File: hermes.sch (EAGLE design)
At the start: 49 parts, among them IC1 MIC5219-3.3BML

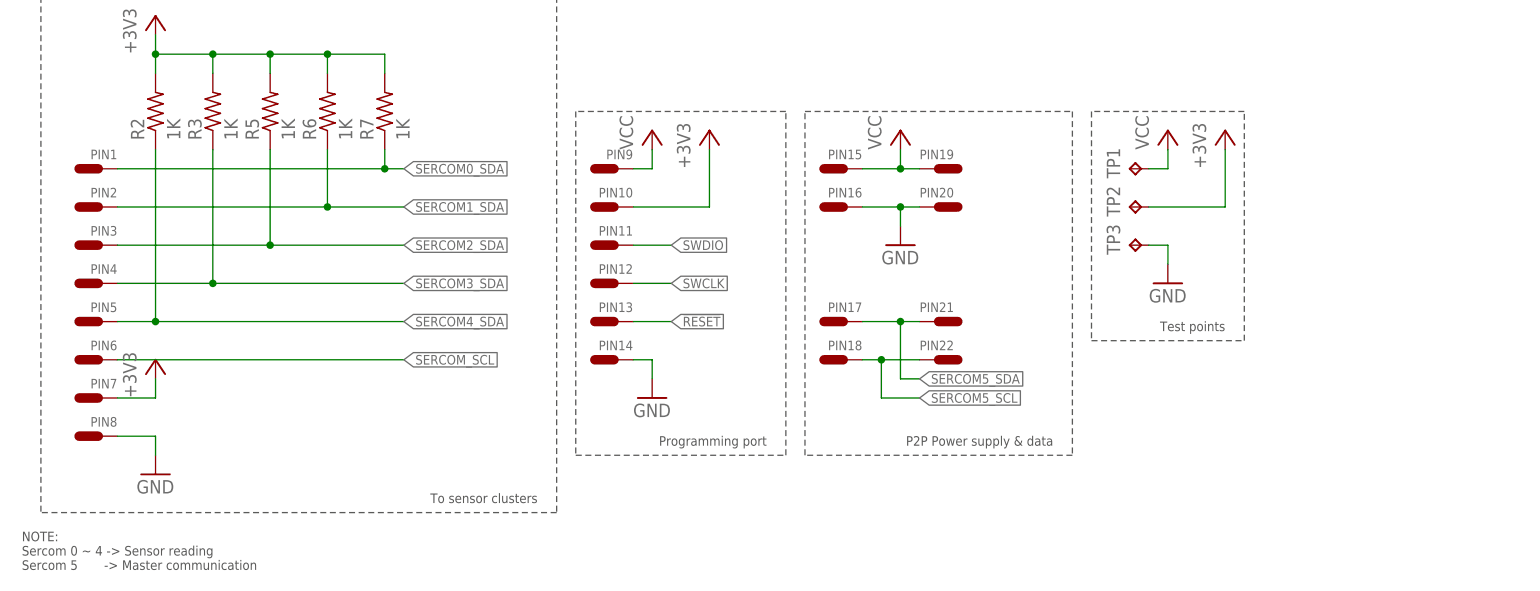
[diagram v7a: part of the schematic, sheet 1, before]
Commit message: -Add correct connectors to library and board
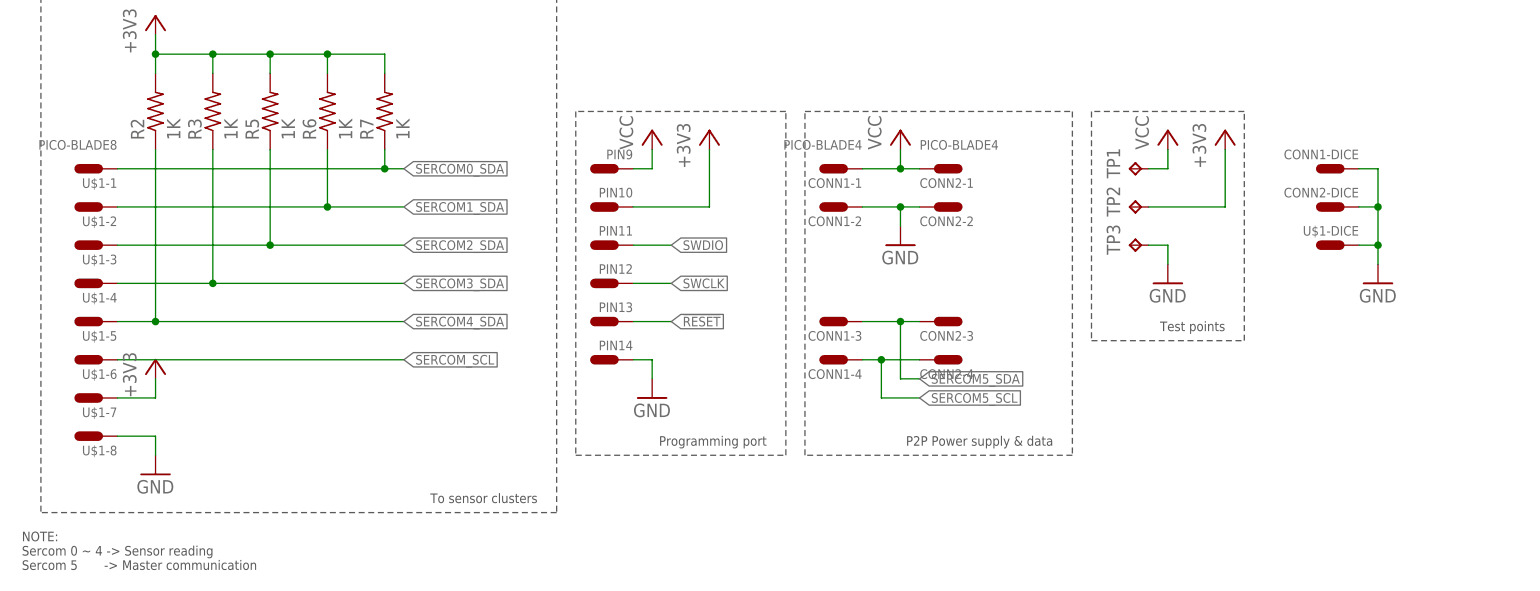
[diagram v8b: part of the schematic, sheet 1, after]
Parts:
- removed PIN1, PIN15, PIN16, PIN17, PIN18, PIN19, PIN2, PIN20, PIN21, PIN22, PIN3, PIN4, PIN5, PIN6, PIN7, PIN8: SINGLE-PIN, Hermes_lib:SINGLE-PIN
- added CONN1, CONN2: PICO-BLADE4, Hermes_lib:PICO-BLADE4
- added U$1: PICO-BLADE8, Hermes_lib:PICO-BLADE8
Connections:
- net +3V3: now also U$1-7.P$1; no longer PIN7.P$1
- net GND: now also CONN1-2.P$1, CONN1-DICE.P$1, CONN2-2.P$1, CONN2-DICE.P$1, U$1-8.P$1, U$1-DICE.P$1; no longer PIN16.P$1, PIN20.P$1, PIN8.P$1
- net SERCOM0_SDA: now also U$1-1.P$1; no longer PIN1.P$1
- net SERCOM1_SDA: now also U$1-2.P$1; no longer PIN2.P$1
- net SERCOM2_SDA: now also U$1-3.P$1; no longer PIN3.P$1
- net SERCOM3_SDA: now also U$1-4.P$1; no longer PIN4.P$1
- net SERCOM4_SDA: now also U$1-5.P$1; no longer PIN5.P$1
- net SERCOM5_SCL: now also CONN1-4.P$1, CONN2-4.P$1; no longer PIN18.P$1, PIN22.P$1
- net SERCOM5_SDA: now also CONN1-3.P$1, CONN2-3.P$1; no longer PIN17.P$1, PIN21.P$1
- net SERCOM_SCL: now also U$1-6.P$1; no longer PIN6.P$1
- net VCC: now also CONN1-1.P$1, CONN2-1.P$1; no longer PIN15.P$1, PIN19.P$1
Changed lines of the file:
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@@
 <part name="P+4" library="supply1" library_urn="urn:adsk.eagle:library:371" deviceset="VCC" device=""/>
 <part name="GND12" library="supply1" library_urn="urn:adsk.eagle:library:371" deviceset="GND" device=""/>
-<part name="PIN6" library="Hermes_lib" deviceset="SINGLE-" device="PIN"/>
-<part name="PIN15" library="Hermes_lib" deviceset="SINGLE-" device="PIN"/>
-<part name="PIN19" library="Hermes_lib" deviceset="SINGLE-" device="PIN"/>
-<part name="PIN16" library="Hermes_lib" deviceset="SINGLE-" device="PIN"/>
-<part name="PIN20" library="Hermes_lib" deviceset="SINGLE-" device="PIN"/>
-<part name="PIN17" library="Hermes_lib" deviceset="SINGLE-" device="PIN"/>
-<part name="PIN21" library="Hermes_lib" deviceset="SINGLE-" device="PIN"/>
-<part name="PIN18" library="Hermes_lib" deviceset="SINGLE-" device="PIN"/>
-<part name="PIN22" library="Hermes_lib" deviceset="SINGLE-" device="PIN"/>
-<part name="PIN7" library="Hermes_lib" deviceset="SINGLE-" device="PIN"/>
-<part name="PIN8" library="Hermes_lib" deviceset="SINGLE-" device="PIN"/>
 <part name="+3V32" library="supply1" library_urn="urn:adsk.eagle:library:371" deviceset="+3V3" device=""/>
 <part name="GND3" library="supply1" library_urn="urn:adsk.eagle:library:371" deviceset="GND" device=""/>
 <part name="P+3" library="supply1" library_urn="urn:adsk.eagle:library:371" deviceset="VCC" device=""/>
 <part name="GND11" library="supply1" library_urn="urn:adsk.eagle:library:371" deviceset="GND" device=""/>
-<part name="PIN1" library="Hermes_lib" deviceset="SINGLE-" device="PIN"/>
-<part name="PIN2" library="Hermes_lib" deviceset="SINGLE-" device="PIN"/>
-<part name="PIN3" library="Hermes_lib" deviceset="SINGLE-" device="PIN"/>
-<part name="PIN4" library="Hermes_lib" deviceset="SINGLE-" device="PIN"/>
-<part name="PIN5" library="Hermes_lib" deviceset="SINGLE-" device="PIN"/>
+<part name="CONN1" library="Hermes_lib" deviceset="PICO-BLADE4" device=""/>
+<part name="CONN2" library="Hermes_lib" deviceset="PICO-BLADE4" device=""/>
+<part name="U$1" library="Hermes_lib" deviceset="PICO-BLADE8" device=""/>
+<part name="GND14" library="supply1" library_urn="urn:adsk.eagle:library:371" deviceset="GND" device=""/>
 </parts>
 <sheets>
@@
 <instance part="P+4" gate="VCC" x="160.02" y="66.04"/>
 <instance part="GND12" gate="1" x="160.02" y="45.72"/>
-<instance part="PIN6" gate="G$1" x="20.32" y="35.56" rot="R180"/>
-<instance part="PIN15" gate="G$1" x="119.38" y="60.96" rot="R180"/>
-<instance part="PIN19" gate="G$1" x="127" y="60.96" rot="MR180"/>
-<instance part="PIN16" gate="G$1" x="119.38" y="55.88" rot="R180"/>
-<instance part="PIN20" gate="G$1" x="127" y="55.88" rot="MR180"/>
-<instance part="PIN17" gate="G$1" x="119.38" y="40.64" rot="R180"/>
-<instance part="PIN21" gate="G$1" x="127" y="40.64" rot="MR180"/>
-<instance part="PIN18" gate="G$1" x="119.38" y="35.56" rot="R180"/>
-<instance part="PIN22" gate="G$1" x="127" y="35.56" rot="MR180"/>
-<instance part="PIN7" gate="G$1" x="20.32" y="30.48" rot="R180"/>
-<instance part="PIN8" gate="G$1" x="20.32" y="25.4" rot="R180"/>
 <instance part="+3V32" gate="G$1" x="25.4" y="35.56"/>
 <instance part="GND3" gate="1" x="25.4" y="20.32"/>
 <instance part="P+3" gate="VCC" x="124.46" y="66.04"/>
 <instance part="GND11" gate="1" x="124.46" y="50.8"/>
-<instance part="PIN1" gate="G$1" x="20.32" y="60.96" rot="R180"/>
-<instance part="PIN2" gate="G$1" x="20.32" y="55.88" rot="R180"/>
-<instance part="PIN3" gate="G$1" x="20.32" y="50.8" rot="R180"/>
-<instance part="PIN4" gate="G$1" x="20.32" y="45.72" rot="R180"/>
-<instance part="PIN5" gate="G$1" x="20.32" y="40.64" rot="R180"/>
+<instance part="CONN1" gate="-1" x="119.38" y="60.96" rot="MR0"/>
+<instance part="CONN1" gate="-2" x="119.38" y="55.88" rot="MR0"/>
+<instance part="CONN1" gate="-3" x="119.38" y="40.64" rot="MR0"/>
+<instance part="CONN1" gate="-4" x="119.38" y="35.56" rot="MR0"/>
+<instance part="CONN2" gate="-1" x="127" y="60.96"/>
+<instance part="CONN2" gate="-2" x="127" y="55.88"/>
+<instance part="CONN2" gate="-3" x="127" y="40.64"/>
+<instance part="CONN2" gate="-4" x="127" y="35.56"/>
+<instance part="U$1" gate="-1" x="20.32" y="60.96" rot="MR0"/>
+<instance part="U$1" gate="-2" x="20.32" y="55.88" rot="MR0"/>
+<instance part="U$1" gate="-3" x="20.32" y="50.8" rot="MR0"/>
+<instance part="U$1" gate="-4" x="20.32" y="45.72" rot="MR0"/>
+<instance part="U$1" gate="-5" x="20.32" y="40.64" rot="MR0"/>
+<instance part="U$1" gate="-6" x="20.32" y="35.56" rot="MR0"/>
+<instance part="U$1" gate="-7" x="20.32" y="30.48" rot="MR0"/>
+<instance part="U$1" gate="-8" x="20.32" y="25.4" rot="MR0"/>
+<instance part="CONN1" gate="-DICE" x="185.42" y="60.96" rot="R180"/>
+<instance part="CONN2" gate="-DICE" x="185.42" y="55.88" rot="R180"/>
+<instance part="U$1" gate="-DICE" x="185.42" y="50.8" rot="R180"/>
+<instance part="GND14" gate="1" x="187.96" y="45.72"/>
 </instances>
 <busses>
@@
 </segment>
 <segment>
-<pinref part="PIN7" gate="G$1" pin="P$1"/>
 <pinref part="+3V32" gate="G$1" pin="+3V3"/>
 <wire x1="20.32" y1="30.48" x2="25.4" y2="30.48" width="0.1524" layer="91"/>
 <wire x1="25.4" y1="30.48" x2="25.4" y2="33.02" width="0.1524" layer="91"/>
+<pinref part="U$1" gate="-7" pin="P$1"/>
 </segment>
 </net>
@@
 </segment>
 <segment>
-<pinref part="PIN20" gate="G$1" pin="P$1"/>
-<pinref part="PIN16" gate="G$1" pin="P$1"/>
 <wire x1="127" y1="55.88" x2="124.46" y2="55.88" width="0.1524" layer="91"/>
 <pinref part="GND11" gate="1" pin="GND"/>
@@
 <wire x1="124.46" y1="55.88" x2="124.46" y2="53.34" width="0.1524" layer="91"/>
 <junction x="124.46" y="55.88"/>
-</segment>
-<segment>
-<pinref part="PIN8" gate="G$1" pin="P$1"/>
+<pinref part="CONN1" gate="-2" pin="P$1"/>
+<pinref part="CONN2" gate="-2" pin="P$1"/>
+</segment>
+<segment>
 <pinref part="GND3" gate="1" pin="GND"/>
 <wire x1="20.32" y1="25.4" x2="25.4" y2="25.4" width="0.1524" layer="91"/>
 <wire x1="25.4" y1="25.4" x2="25.4" y2="22.86" width="0.1524" layer="91"/>
+<pinref part="U$1" gate="-8" pin="P$1"/>
+</segment>
+<segment>
+<pinref part="CONN1" gate="-DICE" pin="P$1"/>
+<pinref part="GND14" gate="1" pin="GND"/>
+<wire x1="185.42" y1="60.96" x2="187.96" y2="60.96" width="0.1524" layer="91"/>
+<wire x1="187.96" y1="60.96" x2="187.96" y2="55.88" width="0.1524" layer="91"/>
+<pinref part="CONN2" gate="-DICE" pin="P$1"/>
+<wire x1="187.96" y1="55.88" x2="187.96" y2="50.8" width="0.1524" layer="91"/>
+<wire x1="187.96" y1="50.8" x2="187.96" y2="48.26" width="0.1524" layer="91"/>
+<wire x1="185.42" y1="55.88" x2="187.96" y2="55.88" width="0.1524" layer="91"/>
+<junction x="187.96" y="55.88"/>
+<pinref part="U$1" gate="-DICE" pin="P$1"/>
+<wire x1="185.42" y1="50.8" x2="187.96" y2="50.8" width="0.1524" layer="91"/>
+<junction x="187.96" y="50.8"/>
 </segment>
 </net>
@@
 </segment>
 <segment>
-<pinref part="PIN15" gate="G$1" pin="P$1"/>
-<pinref part="PIN19" gate="G$1" pin="P$1"/>
 <wire x1="119.38" y1="60.96" x2="124.46" y2="60.96" width="0.1524" layer="91"/>
 <pinref part="P+3" gate="VCC" pin="VCC"/>
@@
 <wire x1="124.46" y1="63.5" x2="124.46" y2="60.96" width="0.1524" layer="91"/>
 <junction x="124.46" y="60.96"/>
+<pinref part="CONN1" gate="-1" pin="P$1"/>
+<pinref part="CONN2" gate="-1" pin="P$1"/>
 </segment>
 </net>
@@
 <net name="SERCOM5_SDA" class="0">
 <segment>
-<pinref part="PIN17" gate="G$1" pin="P$1"/>
-<pinref part="PIN21" gate="G$1" pin="P$1"/>
 <wire x1="119.38" y1="40.64" x2="124.46" y2="40.64" width="0.1524" layer="91"/>
 <wire x1="124.46" y1="40.64" x2="127" y2="40.64" width="0.1524" layer="91"/>
@@
 <wire x1="124.46" y1="33.02" x2="127" y2="33.02" width="0.1524" layer="91"/>
 <label x="127" y="33.02" size="1.27" layer="95" xref="yes"/>
+<pinref part="CONN1" gate="-3" pin="P$1"/>
+<pinref part="CONN2" gate="-3" pin="P$1"/>
 </segment>
 </net>
@@
 <net name="SERCOM_SCL" class="0">
 <segment>
-<pinref part="PIN6" gate="G$1" pin="P$1"/>
 <wire x1="20.32" y1="35.56" x2="58.42" y2="35.56" width="0.1524" layer="91"/>
 <label x="58.42" y="35.56" size="1.27" layer="95" xref="yes"/>
+<pinref part="U$1" gate="-6" pin="P$1"/>
 </segment>
 </net>
 <net name="SERCOM5_SCL" class="0">
 <segment>
-<pinref part="PIN22" gate="G$1" pin="P$1"/>
-<pinref part="PIN18" gate="G$1" pin="P$1"/>
 <wire x1="127" y1="35.56" x2="121.92" y2="35.56" width="0.1524" layer="91"/>
 <wire x1="121.92" y1="35.56" x2="119.38" y2="35.56" width="0.1524" layer="91"/>
@@
 <wire x1="121.92" y1="30.48" x2="127" y2="30.48" width="0.1524" layer="91"/>
 <label x="127" y="30.48" size="1.27" layer="95" xref="yes"/>
+<pinref part="CONN1" gate="-4" pin="P$1"/>
+<pinref part="CONN2" gate="-4" pin="P$1"/>
 </segment>
 </net>
@@
 <wire x1="20.32" y1="60.96" x2="55.88" y2="60.96" width="0.1524" layer="91"/>
 <junction x="55.88" y="60.96"/>
-<pinref part="PIN1" gate="G$1" pin="P$1"/>
+<pinref part="U$1" gate="-1" pin="P$1"/>
 </segment>
 </net>
@@
 <wire x1="20.32" y1="55.88" x2="48.26" y2="55.88" width="0.1524" layer="91"/>
 <junction x="48.26" y="55.88"/>
-<pinref part="PIN2" gate="G$1" pin="P$1"/>
+<pinref part="U$1" gate="-2" pin="P$1"/>
 </segment>
 </net>
@@
 <wire x1="20.32" y1="50.8" x2="40.64" y2="50.8" width="0.1524" layer="91"/>
 <junction x="40.64" y="50.8"/>
-<pinref part="PIN3" gate="G$1" pin="P$1"/>
+<pinref part="U$1" gate="-3" pin="P$1"/>
 </segment>
 </net>
@@
 <wire x1="20.32" y1="45.72" x2="33.02" y2="45.72" width="0.1524" layer="91"/>
 <junction x="33.02" y="45.72"/>
-<pinref part="PIN4" gate="G$1" pin="P$1"/>
+<pinref part="U$1" gate="-4" pin="P$1"/>
 </segment>
 </net>
@@
 <wire x1="20.32" y1="40.64" x2="25.4" y2="40.64" width="0.1524" layer="91"/>
 <junction x="25.4" y="40.64"/>
-<pinref part="PIN5" gate="G$1" pin="P$1"/>
-</segment>
-</net>
+<pinref part="U$1" gate="-5" pin="P$1"/>
+</segment>
+</net>
